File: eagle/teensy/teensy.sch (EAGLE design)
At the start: 4 parts

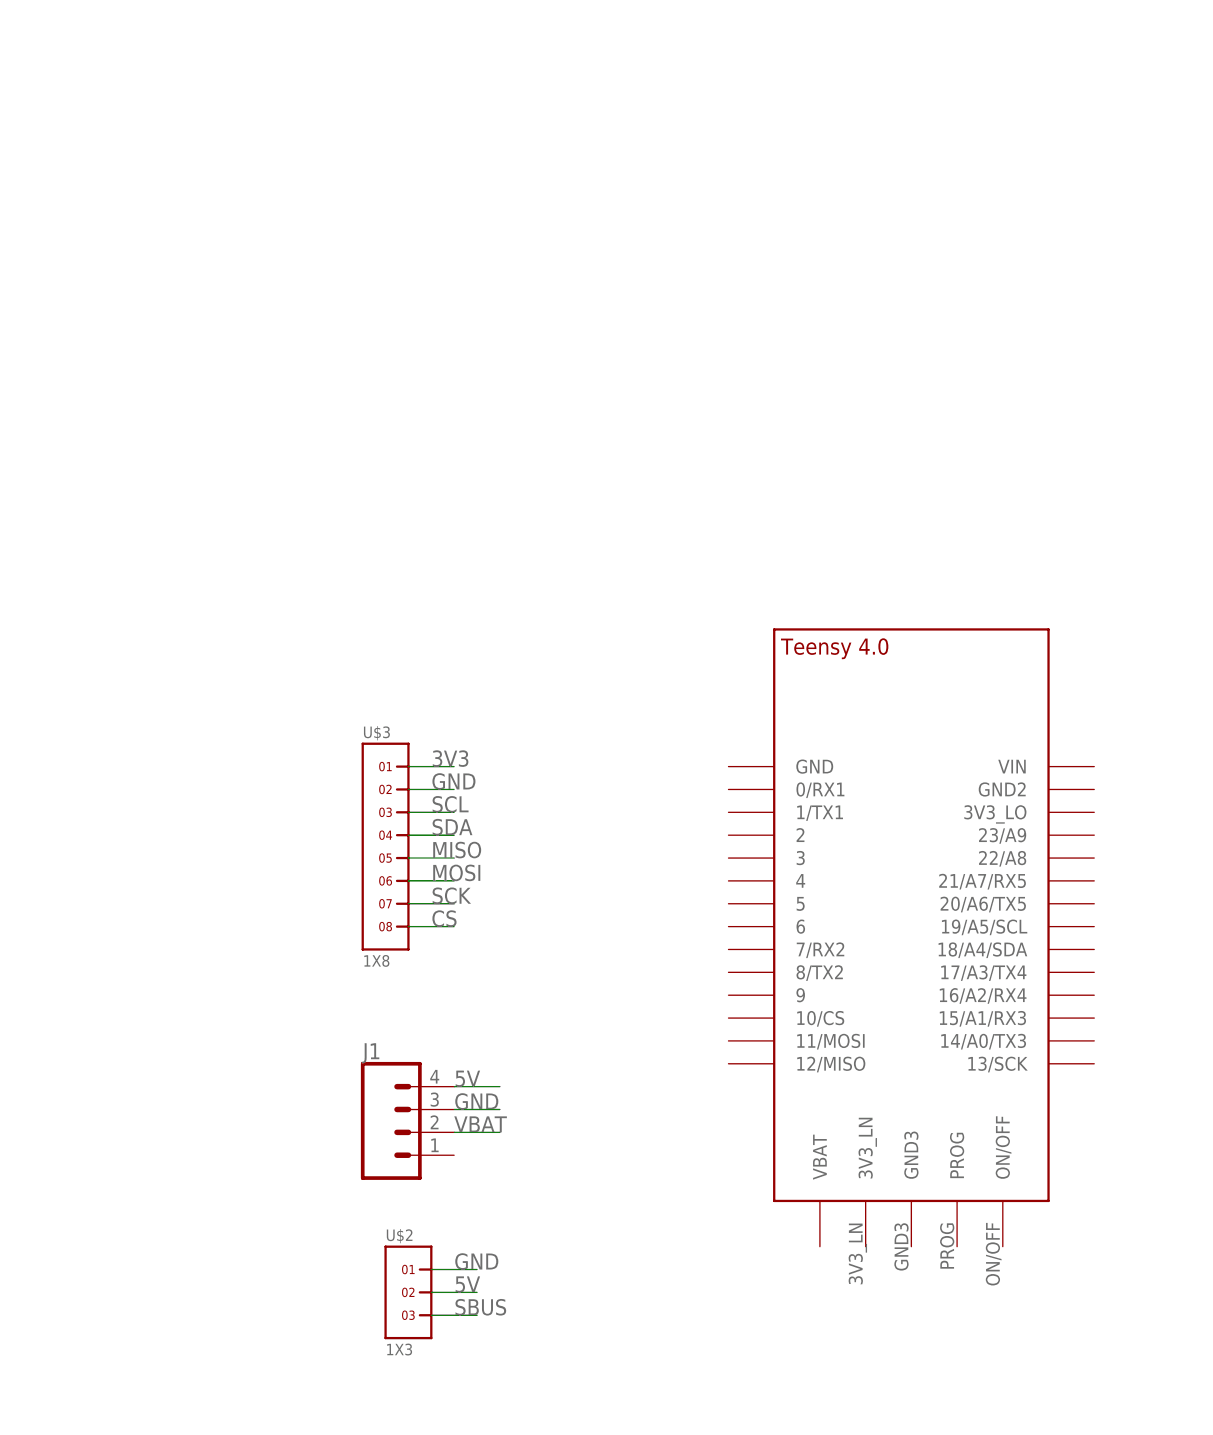
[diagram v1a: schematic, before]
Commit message: modified:   eagle/teensy/teensy.brd
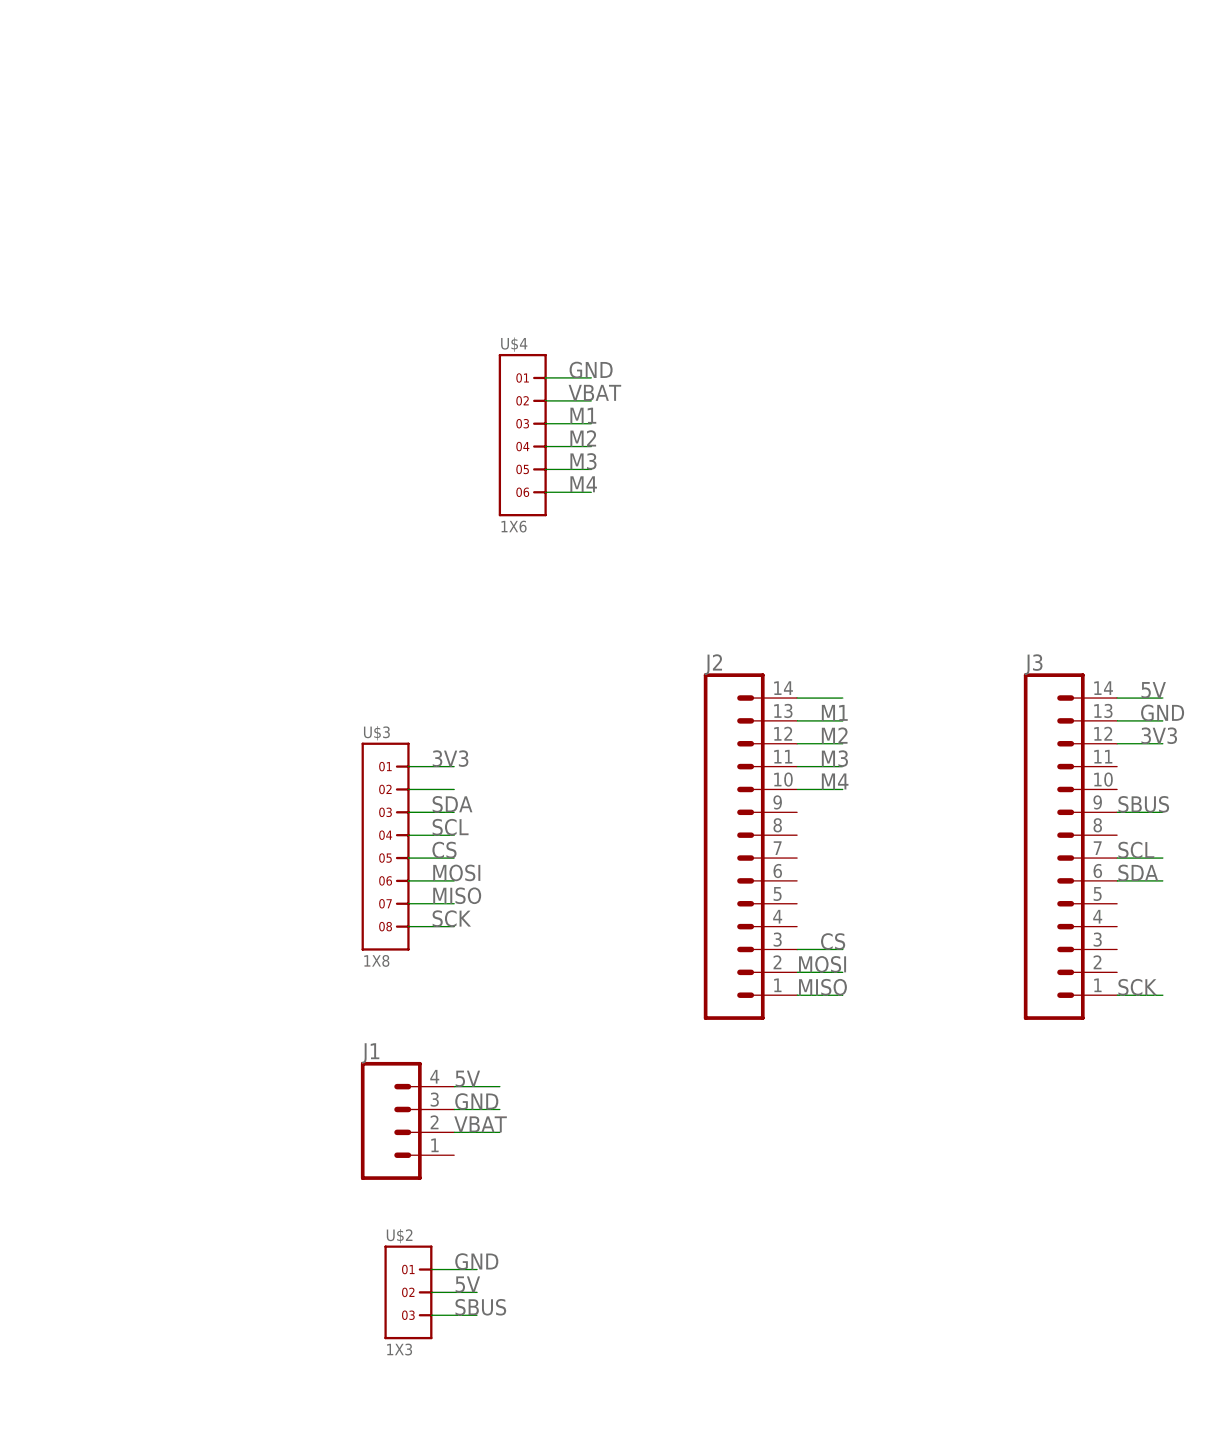
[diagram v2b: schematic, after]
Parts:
- removed U$1: TEENSY_4.0, TEENSY 4.0:TEENSY_4.0
- added J2, J3: (no value), SparkFun-Connectors:CONN_14NO_SILK
- added U$4: 1X6, headers(2mm):1X6
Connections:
- new net M1: J2.13, U$4.3
- new net M2: J2.12, U$4.4
- new net M3: J2.11, U$4.5
- new net M4: J2.10, U$4.6
- net 3V3: now also J3.12
- net 5V: now also J3.14
- net CS: now also J2.3, U$3.5; no longer U$3.8
- net GND: now also J2.14, J3.13, U$4.1
- net MISO: now also J2.1, U$3.7; no longer U$3.5
- net MOSI: now also J2.2
- net SBUS: now also J3.9
- net SCK: now also J3.1, U$3.8; no longer U$3.7
- net SCL: now also J3.7, U$3.4; no longer U$3.3
- net SDA: now also J3.6, U$3.3; no longer U$3.4
- net VBAT: now also U$4.2
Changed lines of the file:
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@@
 <?xml version="1.0" encoding="utf-8"?>
 <!DOCTYPE eagle SYSTEM "eagle.dtd">
-<eagle version="9.6.2">
+<eagle version="9.1.1">
 <drawing>
 <settings>
@@
 </classes>
 <parts>
-<part name="U$1" library="TEENSY 4.0" deviceset="TEENSY_4.0" device=""/>
 <part name="J1" library="SparkFun-Connectors" deviceset="CONN_04" device="1X04_NO_SILK"/>
 <part name="U$2" library="headers(2mm)" deviceset="1X3" device=""/>
 <part name="U$3" library="headers(2mm)" deviceset="1X8" device=""/>
+<part name="U$4" library="headers(2mm)" deviceset="1X6" device=""/>
+<part name="J2" library="SparkFun-Connectors" deviceset="CONN_14" device="NO_SILK"/>
+<part name="J3" library="SparkFun-Connectors" deviceset="CONN_14" device="NO_SILK"/>
 </parts>
 <sheets>
@@
 </plain>
 <instances>
-<instance part="U$1" gate="G$1" x="86.36" y="63.5" smashed="yes"/>
 <instance part="J1" gate="J1" x="30.48" y="35.56" smashed="yes">
 <attribute name="VALUE" x="25.4" y="28.194" size="1.778" layer="96" font="vector"/>
@@
 <attribute name="VALUE" x="25.4" y="53.975" size="1.27" layer="96" font="vector"/>
 </instance>
+<instance part="U$4" gate="G$1" x="43.18" y="111.76"/>
+<instance part="J2" gate="G$1" x="63.5" y="68.58"/>
+<instance part="J3" gate="G$1" x="99.06" y="68.58"/>
 </instances>
 <busses>
@@
 <net name="GND" class="0">
 <segment>
+<pinref part="U$2" gate="G$1" pin="1"/>
+<wire x1="33.02" y1="20.32" x2="38.1" y2="20.32" width="0.1524" layer="91"/>
+<label x="35.56" y="20.32" size="1.778" layer="95"/>
+</segment>
+<segment>
+<pinref part="U$3" gate="G$1" pin="2"/>
+<wire x1="30.48" y1="73.66" x2="35.56" y2="73.66" width="0.1524" layer="91"/>
+</segment>
+<segment>
+<pinref part="U$4" gate="G$1" pin="1"/>
+<wire x1="45.72" y1="119.38" x2="50.8" y2="119.38" width="0.1524" layer="91"/>
+<label x="48.26" y="119.38" size="1.778" layer="95"/>
+</segment>
+<segment>
+<pinref part="J2" gate="G$1" pin="14"/>
+<wire x1="73.66" y1="83.82" x2="78.74" y2="83.82" width="0.1524" layer="91"/>
+</segment>
+<segment>
+<pinref part="J3" gate="G$1" pin="13"/>
+<wire x1="109.22" y1="81.28" x2="114.3" y2="81.28" width="0.1524" layer="91"/>
+<label x="111.76" y="81.28" size="1.778" layer="95"/>
+</segment>
+<segment>
 <pinref part="J1" gate="J1" pin="3"/>
 <wire x1="35.56" y1="38.1" x2="40.64" y2="38.1" width="0.1524" layer="91"/>
 <label x="35.56" y="38.1" size="1.778" layer="95"/>
 </segment>
-<segment>
-<pinref part="U$2" gate="G$1" pin="1"/>
-<wire x1="33.02" y1="20.32" x2="38.1" y2="20.32" width="0.1524" layer="91"/>
-<label x="35.56" y="20.32" size="1.778" layer="95"/>
-</segment>
-<segment>
-<pinref part="U$3" gate="G$1" pin="2"/>
-<wire x1="30.48" y1="73.66" x2="35.56" y2="73.66" width="0.1524" layer="91"/>
-<label x="33.02" y="73.66" size="1.778" layer="95"/>
-</segment>
 </net>
 <net name="5V" class="0">
@@
 <label x="35.56" y="17.78" size="1.778" layer="95"/>
 </segment>
+<segment>
+<pinref part="J3" gate="G$1" pin="14"/>
+<wire x1="109.22" y1="83.82" x2="114.3" y2="83.82" width="0.1524" layer="91"/>
+<label x="111.76" y="83.82" size="1.778" layer="95"/>
+</segment>
 </net>
 <net name="VBAT" class="0">
@@
 <label x="35.56" y="35.56" size="1.778" layer="95"/>
 </segment>
+<segment>
+<pinref part="U$4" gate="G$1" pin="2"/>
+<wire x1="45.72" y1="116.84" x2="50.8" y2="116.84" width="0.1524" layer="91"/>
+<label x="48.26" y="116.84" size="1.778" layer="95"/>
+</segment>
 </net>
 <net name="SBUS" class="0">
@@
 <label x="35.56" y="15.24" size="1.778" layer="95"/>
 </segment>
+<segment>
+<pinref part="J3" gate="G$1" pin="9"/>
+<wire x1="109.22" y1="71.12" x2="114.3" y2="71.12" width="0.1524" layer="91"/>
+<label x="109.22" y="71.12" size="1.778" layer="95"/>
+</segment>
 </net>
 <net name="3V3" class="0">
@@
 <label x="33.02" y="76.2" size="1.778" layer="95"/>
 </segment>
-</net>
-<net name="SCL" class="0">
+<segment>
+<pinref part="J3" gate="G$1" pin="12"/>
+<wire x1="109.22" y1="78.74" x2="114.3" y2="78.74" width="0.1524" layer="91"/>
+<label x="111.76" y="78.74" size="1.778" layer="95"/>
+</segment>
+</net>
+<net name="SDA" class="0">
 <segment>
 <pinref part="U$3" gate="G$1" pin="3"/>
@@
 <label x="33.02" y="71.12" size="1.778" layer="95"/>
 </segment>
-</net>
-<net name="SDA" class="0">
+<segment>
+<pinref part="J3" gate="G$1" pin="6"/>
+<wire x1="109.22" y1="63.5" x2="114.3" y2="63.5" width="0.1524" layer="91"/>
+<label x="109.22" y="63.5" size="1.778" layer="95"/>
+</segment>
+</net>
+<net name="MOSI" class="0">
+<segment>
+<pinref part="U$3" gate="G$1" pin="6"/>
+<wire x1="30.48" y1="63.5" x2="35.56" y2="63.5" width="0.1524" layer="91"/>
+<label x="33.02" y="63.5" size="1.778" layer="95"/>
+</segment>
+<segment>
+<pinref part="J2" gate="G$1" pin="2"/>
+<wire x1="73.66" y1="53.34" x2="78.74" y2="53.34" width="0.1524" layer="91"/>
+<label x="73.66" y="53.34" size="1.778" layer="95"/>
+</segment>
+</net>
+<net name="MISO" class="0">
+<segment>
+<pinref part="U$3" gate="G$1" pin="7"/>
+<wire x1="30.48" y1="60.96" x2="35.56" y2="60.96" width="0.1524" layer="91"/>
+<label x="33.02" y="60.96" size="1.778" layer="95"/>
+</segment>
+<segment>
+<pinref part="J2" gate="G$1" pin="1"/>
+<wire x1="73.66" y1="50.8" x2="78.74" y2="50.8" width="0.1524" layer="91"/>
+<label x="73.66" y="50.8" size="1.778" layer="95"/>
+</segment>
+</net>
+<net name="CS" class="0">
+<segment>
+<pinref part="U$3" gate="G$1" pin="5"/>
+<wire x1="30.48" y1="66.04" x2="35.56" y2="66.04" width="0.1524" layer="91"/>
+<label x="33.02" y="66.04" size="1.778" layer="95"/>
+</segment>
+<segment>
+<pinref part="J2" gate="G$1" pin="3"/>
+<wire x1="73.66" y1="55.88" x2="78.74" y2="55.88" width="0.1524" layer="91"/>
+<label x="76.2" y="55.88" size="1.778" layer="95"/>
+</segment>
+</net>
+<net name="SCL" class="0">
 <segment>
 <pinref part="U$3" gate="G$1" pin="4"/>
@@
 <label x="33.02" y="68.58" size="1.778" layer="95"/>
 </segment>
-</net>
-<net name="MISO" class="0">
-<segment>
-<pinref part="U$3" gate="G$1" pin="5"/>
-<wire x1="30.48" y1="66.04" x2="35.56" y2="66.04" width="0.1524" layer="91"/>
-<label x="33.02" y="66.04" size="1.778" layer="95"/>
-</segment>
-</net>
-<net name="MOSI" class="0">
-<segment>
-<pinref part="U$3" gate="G$1" pin="6"/>
-<wire x1="30.48" y1="63.5" x2="35.56" y2="63.5" width="0.1524" layer="91"/>
-<label x="33.02" y="63.5" size="1.778" layer="95"/>
+<segment>
+<pinref part="J3" gate="G$1" pin="7"/>
+<wire x1="109.22" y1="66.04" x2="114.3" y2="66.04" width="0.1524" layer="91"/>
+<label x="109.22" y="66.04" size="1.778" layer="95"/>
 </segment>
 </net>
 <net name="SCK" class="0">
-<segment>
-<pinref part="U$3" gate="G$1" pin="7"/>
-<wire x1="30.48" y1="60.96" x2="35.56" y2="60.96" width="0.1524" layer="91"/>
-<label x="33.02" y="60.96" size="1.778" layer="95"/>
-</segment>
-</net>
-<net name="CS" class="0">
 <segment>
 <pinref part="U$3" gate="G$1" pin="8"/>
 <wire x1="30.48" y1="58.42" x2="35.56" y2="58.42" width="0.1524" layer="91"/>
 <label x="33.02" y="58.42" size="1.778" layer="95"/>
+</segment>
+<segment>
+<pinref part="J3" gate="G$1" pin="1"/>
+<wire x1="109.22" y1="50.8" x2="114.3" y2="50.8" width="0.1524" layer="91"/>
+<label x="109.22" y="50.8" size="1.778" layer="95"/>
+</segment>
+</net>
+<net name="M1" class="0">
+<segment>
+<pinref part="U$4" gate="G$1" pin="3"/>
+<wire x1="45.72" y1="114.3" x2="50.8" y2="114.3" width="0.1524" layer="91"/>
+<label x="48.26" y="114.3" size="1.778" layer="95"/>
+</segment>
+<segment>
+<pinref part="J2" gate="G$1" pin="13"/>
+<wire x1="73.66" y1="81.28" x2="78.74" y2="81.28" width="0.1524" layer="91"/>
+<label x="76.2" y="81.28" size="1.778" layer="95"/>
+</segment>
+</net>
+<net name="M2" class="0">
+<segment>
+<pinref part="U$4" gate="G$1" pin="4"/>
+<wire x1="45.72" y1="111.76" x2="50.8" y2="111.76" width="0.1524" layer="91"/>
+<label x="48.26" y="111.76" size="1.778" layer="95"/>
+</segment>
+<segment>
+<pinref part="J2" gate="G$1" pin="12"/>
+<wire x1="73.66" y1="78.74" x2="78.74" y2="78.74" width="0.1524" layer="91"/>
+<label x="76.2" y="78.74" size="1.778" layer="95"/>
+</segment>
+</net>
+<net name="M3" class="0">
+<segment>
+<pinref part="U$4" gate="G$1" pin="5"/>
+<wire x1="45.72" y1="109.22" x2="50.8" y2="109.22" width="0.1524" layer="91"/>
+<label x="48.26" y="109.22" size="1.778" layer="95"/>
+</segment>
+<segment>
+<pinref part="J2" gate="G$1" pin="11"/>
+<wire x1="73.66" y1="76.2" x2="78.74" y2="76.2" width="0.1524" layer="91"/>
+<label x="76.2" y="76.2" size="1.778" layer="95"/>
+</segment>
+</net>
+<net name="M4" class="0">
+<segment>
+<pinref part="U$4" gate="G$1" pin="6"/>
+<wire x1="45.72" y1="106.68" x2="50.8" y2="106.68" width="0.1524" layer="91"/>
+<label x="48.26" y="106.68" size="1.778" layer="95"/>
+</segment>
+<segment>
+<pinref part="J2" gate="G$1" pin="10"/>
+<wire x1="73.66" y1="73.66" x2="78.74" y2="73.66" width="0.1524" layer="91"/>
+<label x="76.2" y="73.66" size="1.778" layer="95"/>
 </segment>
 </net>
@@
 </schematic>
 </drawing>
-<compatibility>
-<note version="6.3" minversion="6.2.2" severity="warning">
-Since Version 6.2.2 text objects can contain more than one line,
-which will not be processed correctly with this version.
-</note>
-</compatibility>
 </eagle>

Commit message: modified:   eagle/teensy/teensy.brd
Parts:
- added D1: WHITE, SparkFun-LED:LED-WHITE0603
- added R1: 22, SparkFun-Resistors:22OHM-0603-1/10W-1%
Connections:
- new net R1: J2.4, R1.1
- new net R2: D1.A, R1.2
- net GND: now also D1.C
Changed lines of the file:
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@@
 <part name="J2" library="SparkFun-Connectors" deviceset="CONN_14" device="NO_SILK"/>
 <part name="J3" library="SparkFun-Connectors" deviceset="CONN_14" device="NO_SILK"/>
+<part name="D1" library="SparkFun-LED" deviceset="LED-WHITE" device="0603" value="WHITE"/>
+<part name="R1" library="SparkFun-Resistors" deviceset="22OHM" device="-0603-1/10W-1%" value="22"/>
 </parts>
 <sheets>
@@
 <instance part="J2" gate="G$1" x="63.5" y="68.58"/>
 <instance part="J3" gate="G$1" x="99.06" y="68.58"/>
+<instance part="D1" gate="G$1" x="93.98" y="15.24" smashed="yes" rot="R90">
+<attribute name="VALUE" x="98.552" y="17.145" size="1.778" layer="96" font="vector" rot="R180" align="top-left"/>
+</instance>
+<instance part="R1" gate="G$1" x="88.9" y="5.08" smashed="yes"/>
 </instances>
 <busses>
@@
 <pinref part="J2" gate="G$1" pin="14"/>
 <wire x1="73.66" y1="83.82" x2="78.74" y2="83.82" width="0.1524" layer="91"/>
+<label x="76.2" y="83.82" size="1.778" layer="95"/>
 </segment>
 <segment>
@@
 <label x="35.56" y="38.1" size="1.778" layer="95"/>
 </segment>
+<segment>
+<pinref part="D1" gate="G$1" pin="C"/>
+<wire x1="99.06" y1="15.24" x2="104.14" y2="15.24" width="0.1524" layer="91"/>
+<label x="99.06" y="15.24" size="1.778" layer="95"/>
+</segment>
 </net>
 <net name="5V" class="0">
@@
 </segment>
 </net>
+<net name="R2" class="0">
+<segment>
+<pinref part="D1" gate="G$1" pin="A"/>
+<wire x1="91.44" y1="15.24" x2="86.36" y2="15.24" width="0.1524" layer="91"/>
+<label x="86.36" y="15.24" size="1.778" layer="95"/>
+</segment>
+<segment>
+<pinref part="R1" gate="G$1" pin="2"/>
+<wire x1="93.98" y1="5.08" x2="99.06" y2="5.08" width="0.1524" layer="91"/>
+<label x="93.98" y="5.08" size="1.778" layer="95"/>
+</segment>
+</net>
+<net name="R1" class="0">
+<segment>
+<pinref part="R1" gate="G$1" pin="1"/>
+<wire x1="83.82" y1="5.08" x2="78.74" y2="5.08" width="0.1524" layer="91"/>
+<label x="78.74" y="5.08" size="1.778" layer="95"/>
+</segment>
+<segment>
+<pinref part="J2" gate="G$1" pin="4"/>
+<wire x1="73.66" y1="58.42" x2="78.74" y2="58.42" width="0.1524" layer="91"/>
+<label x="76.2" y="58.42" size="1.778" layer="95"/>
+</segment>
+</net>
